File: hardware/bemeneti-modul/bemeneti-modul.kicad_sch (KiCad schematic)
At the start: 112 parts, among them J301 IN0, J302 IN1, J303 IN2, J304 IN3, J305 IN4, J306 IN5, J307 IN6, J308 IN7, J309 IN8, J310 IN9, J311 IN10, J312 IN11, J313 IN12, J314 IN13, J315 IN14, J316 IN15, J320 I2C KÜLSŐ, U301 AP2112K-3.3TRG1, U302 HDC3020DEFR, U303 TPD4E05U06DQAR, U304 TPD4E05U06DQAR, U305 TPD4E05U06DQAR, U306 TPD4E05U06DQAR, U307 TPD4E05U06DQAR

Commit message: Hardver: szakértői javítások (D74–D77), STM32L433 + SN65HVD230 + GND-ági polaritásvédelem (D78–D81), teljes ellenőrzés
- D74–D77: busz-GND ellenállás, CAN-fojtó-hely, TVS a +5V_BUCK-on és a VUSB-n, bemenetvédelem,
  230 V-os és antenna-tiltás a NYÁK-on, SCT-jack footprint
- D78–D80: modul-MCU STM32L433RCT3 (VIN_SENSE PB1, LED: TIM15/TIM16, I_SENSE PA3), modul-transceiver
  SN65HVD230, N-FET a GND-ágban (vezérlő Q1, LED Q201, relé Q100), MCP9701A, táp-LED a +5V-ról,
  2 oz a LED-/relémodulon, AP2112K marad; D81 javaslat (TPD4E02B04 a bemeneteken)
- CubeMX-projektek L433-ra, fejsoros kódgenerálással ellenőrizve (minden periféria inicializálódik)
- gen/ellenorzes.py (ERC, láb ↔ pad, modulmag, CubeMX, polaritásvédelem, NYÁK ↔ rajz, DRC) – 0 hiba
- gen/bom.sh + bom/*.csv darabjegyzék; docs/komponenslista.md a konzulensnek
- kontextus: DONTESEK D74–D81, specifikációk, ATTEKINTES, NAPLO, beszerzési lista; alkatrészkészlet-jegyzet (claude.ai)

Co-Authored-By: Claude Opus 5.5 <noreply@anthropic.com>
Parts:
- added R390: 0R, Resistor_SMD:R_1206_3216Metric, symbol Device:R
- R310, R311, R312, R313, R314, R315, R316, R317, R318, R319, R320, R321, R322, R323, R324, R325: value 1k -> 10k; Megjegyzés (none) -> soros: 24 V-os félrekötésnél ~2 mA az ESD-tömbbe (U303–U306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
- R330, R331, R332, R333, R334, R335, R336, R337, R338, R339, R340, R341, R342, R343, R344, R345: Megjegyzés (none) -> felhúzás a csatlakozó oldalán (D75); 12/24 V-os jelnél kive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
- U302: Megjegyzés (none) -> a ház belsejének klímáját méri (elosztószekrény), nem a szo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
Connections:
- net GND: now also R390.2
- net IN0: no longer R330.2
- net IN1: no longer R331.2
- net IN10: no longer R340.2
- net IN11: no longer R341.2
- net IN12: no longer R342.2
- net IN13: no longer R343.2
- net IN14: no longer R344.2
- net IN15: no longer R345.2
- net IN2: no longer R332.2
- net IN3: no longer R333.2
- net IN4: no longer R334.2
- net IN5: no longer R335.2
- net IN6: no longer R336.2
- net IN7: no longer R337.2
- net IN8: no longer R338.2
- net IN9: no longer R339.2
- net at J306.3 (Pin_3), R315.1: now also R335.2
- net at J301.3 (Pin_3), R310.1: now also R330.2
- net at J315.3 (Pin_3), R324.1: now also R344.2
- net at J302.3 (Pin_3), R311.1: now also R331.2
- net at J309.3 (Pin_3), R318.1: now also R338.2
- net at J311.3 (Pin_3), R320.1: now also R340.2
- net at J307.3 (Pin_3), R316.1: now also R336.2
- net at J304.3 (Pin_3), R313.1: now also R333.2
- net at J312.3 (Pin_3), R321.1: now also R341.2
- net at J305.3 (Pin_3), R314.1: now also R334.2
- net at J314.3 (Pin_3), R323.1: now also R343.2
- net at J313.3 (Pin_3), R322.1: now also R342.2
- net at J303.3 (Pin_3), R312.1: now also R332.2
- net at J310.3 (Pin_3), R319.1: now also R339.2
- net at J308.3 (Pin_3), R317.1: now also R337.2
- net at J316.3 (Pin_3), R325.1: now also R345.2
- new net GND_BUS: R390.1
- no-connect marks 28 -> 26
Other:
- sheet modulmag ports: added GND_BUS, PB1; removed PC6, PC7, PC8
- note added: "2. BEMENETEK (× 16): PH 1 = táp (SUPk), 2 = GND, 3 = JEL → R_fel a 3,3 V-ra (csatlakozó-oldal) → R_s → csomópont (R_le (DNP), C) → MCU; ESD az MCU-oldalon"
- note added: "Alap: R_fel 10k + R_s 10k + C 10n (D75) – félrekötött 24 V-nál ~2 mA az ESD-tömbbe, a láb ~VBR-en (D81!). 12/24 V-os jel: R_fel ki, R_s 68k, R_le 10k; 5 V: R_s 2k2, R_le 3k9."
- note removed: "2. BEMENETEK (× 16): PH 1 = táp (SUPk), 2 = GND, 3 = JEL → R_s → csomópont (R_fel a 3,3 V-ra, R_le (DNP) és C a GND-re) → MCU; ESD az MCU-oldalon (lent)"
- note removed: "Alap: R_s 1k + R_fel 10k + C 10n → érintkező, reed, gomb, open-drain (pl. AH1911), 3,3 V-os kimenet. 12/24 V-os jel: R_s 68k, R_le 10k, R_fel ki."

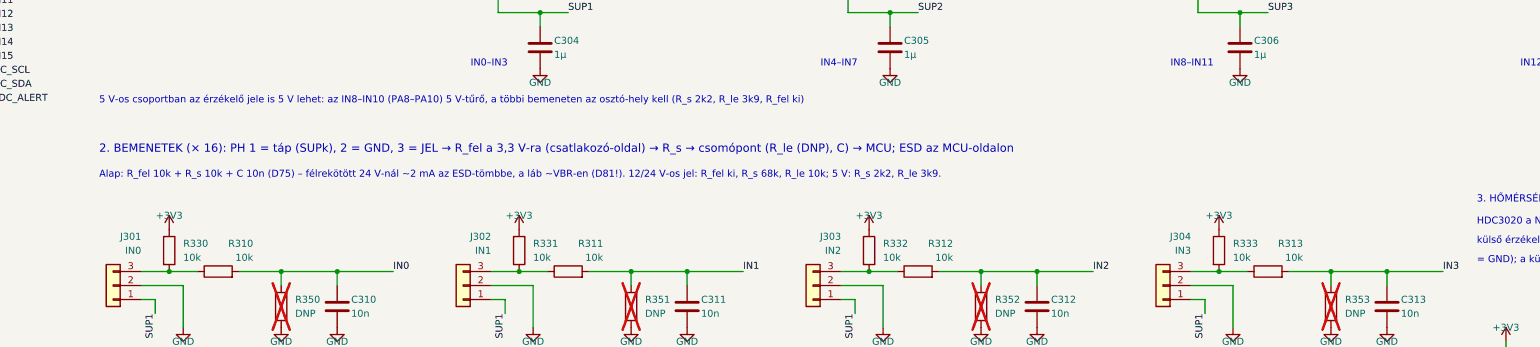
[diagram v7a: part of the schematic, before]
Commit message: Hardver: relékimenet 5,08 mm-es THT sorkapocs (D83), D81 elvetve – marad a TPD4E05U06
Co-Authored-By: Claude Opus 5.5 <noreply@anthropic.com>
Claude-Session: https://claude.ai/code/session_01KVtZMUPbtveTXy9VyJshyt
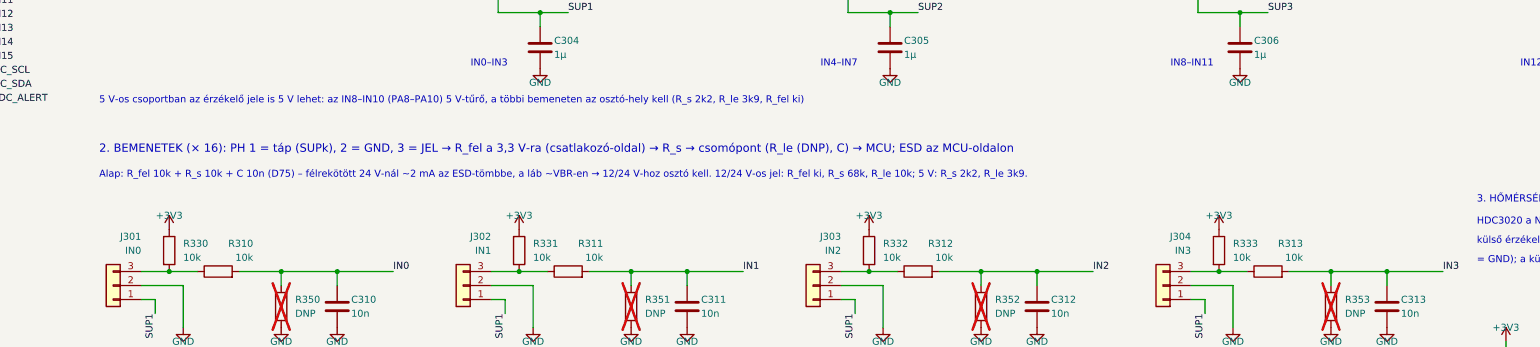
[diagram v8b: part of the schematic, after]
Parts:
- R310, R311, R312, R313, R314, R315, R316, R317, R318, R319, R320, R321, R322, R323, R324, R325: Megjegyzés soros: 24 V-os félrekötésnél ~2 mA az ESD-tömbbe (U303–U306), a láb a letörési feszültségén – D75, D81; 12/24 V-os osztóhoz 68k -> soros: 24 V-os félrekötésnél ~2 mA az ESD-tömbbe (U303–U306), a láb a letörési feszültségén (D75) – 12/24 V-os jelhez osztó (68k)
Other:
- note added: "Alap: R_fel 10k + R_s 10k + C 10n (D75) – félrekötött 24 V-nál ~2 mA az ESD-tömbbe, a láb ~VBR-en → 12/24 V-hoz osztó kell. 12/24 V-os jel: R_fel ki, R_s 68k, R_le 10k; 5 V: R_s 2k2, R_le 3k9."
- note removed: "Alap: R_fel 10k + R_s 10k + C 10n (D75) – félrekötött 24 V-nál ~2 mA az ESD-tömbbe, a láb ~VBR-en (D81!). 12/24 V-os jel: R_fel ki, R_s 68k, R_le 10k; 5 V: R_s 2k2, R_le 3k9."
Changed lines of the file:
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@@
 		)
 	)
-	(text "Alap: R_fel 10k + R_s 10k + C 10n (D75) – félrekötött 24 V-nál ~2 mA az ESD-tömbbe, a láb ~VBR-en (D81!). 12/24 V-os jel: R_fel ki, R_s 68k, R_le 10k; 5 V: R_s 2k2, R_le 3k9."
+	(text "Alap: R_fel 10k + R_s 10k + C 10n (D75) – félrekötött 24 V-nál ~2 mA az ESD-tömbbe, a láb ~VBR-en → 12/24 V-hoz osztó kell. 12/24 V-os jel: R_fel ki, R_s 68k, R_le 10k; 5 V: R_s 2k2, R_le 3k9."
 		(exclude_from_sim no)
 		(at 80 97.5 0)
@@
 			)
 		)
-		(property "Megjegyzés" "soros: 24 V-os félrekötésnél ~2 mA az ESD-tömbbe (U303–U306), a láb a letörési feszültségén – D75, D81; 12/24 V-os osztóhoz 68k"
+		(property "Megjegyzés" "soros: 24 V-os félrekötésnél ~2 mA az ESD-tömbbe (U303–U306), a láb a letörési feszültségén (D75) – 12/24 V-os jelhez osztó (68k)"
 			(at 292.1 172.72 90)
 			(hide yes)
@@
 			)
 		)
-		(property "Megjegyzés" "soros: 24 V-os félrekötésnél ~2 mA az ESD-tömbbe (U303–U306), a láb a letörési feszültségén – D75, D81; 12/24 V-os osztóhoz 68k"
+		(property "Megjegyzés" "soros: 24 V-os félrekötésnél ~2 mA az ESD-tömbbe (U303–U306), a láb a letörési feszültségén (D75) – 12/24 V-os jelhez osztó (68k)"
 			(at 101.6 201.93 90)
 			(hide yes)
@@
 			)
 		)
-		(property "Megjegyzés" "soros: 24 V-os félrekötésnél ~2 mA az ESD-tömbbe (U303–U306), a láb a letörési feszültségén – D75, D81; 12/24 V-os osztóhoz 68k"
+		(property "Megjegyzés" "soros: 24 V-os félrekötésnél ~2 mA az ESD-tömbbe (U303–U306), a láb a letörési feszültségén (D75) – 12/24 V-os jelhez osztó (68k)"
 			(at 228.6 114.3 90)
 			(hide yes)
@@
 			)
 		)
-		(property "Megjegyzés" "soros: 24 V-os félrekötésnél ~2 mA az ESD-tömbbe (U303–U306), a láb a letörési feszültségén – D75, D81; 12/24 V-os osztóhoz 68k"
+		(property "Megjegyzés" "soros: 24 V-os félrekötésnél ~2 mA az ESD-tömbbe (U303–U306), a láb a letörési feszültségén (D75) – 12/24 V-os jelhez osztó (68k)"
 			(at 292.1 201.93 90)
 			(hide yes)
@@
 			)
 		)
-		(property "Megjegyzés" "soros: 24 V-os félrekötésnél ~2 mA az ESD-tömbbe (U303–U306), a láb a letörési feszültségén – D75, D81; 12/24 V-os osztóhoz 68k"
+		(property "Megjegyzés" "soros: 24 V-os félrekötésnél ~2 mA az ESD-tömbbe (U303–U306), a láb a letörési feszültségén (D75) – 12/24 V-os jelhez osztó (68k)"
 			(at 228.6 143.51 90)
 			(hide yes)
@@
 			)
 		)
-		(property "Megjegyzés" "soros: 24 V-os félrekötésnél ~2 mA az ESD-tömbbe (U303–U306), a láb a letörési feszültségén – D75, D81; 12/24 V-os osztóhoz 68k"
+		(property "Megjegyzés" "soros: 24 V-os félrekötésnél ~2 mA az ESD-tömbbe (U303–U306), a láb a letörési feszültségén (D75) – 12/24 V-os jelhez osztó (68k)"
 			(at 292.1 143.51 90)
 			(hide yes)
@@
 			)
 		)
-		(property "Megjegyzés" "soros: 24 V-os félrekötésnél ~2 mA az ESD-tömbbe (U303–U306), a láb a letörési feszültségén – D75, D81; 12/24 V-os osztóhoz 68k"
+		(property "Megjegyzés" "soros: 24 V-os félrekötésnél ~2 mA az ESD-tömbbe (U303–U306), a láb a letörési feszültségén (D75) – 12/24 V-os jelhez osztó (68k)"
 			(at 101.6 172.72 90)
 			(hide yes)
@@
 			)
 		)
-		(property "Megjegyzés" "soros: 24 V-os félrekötésnél ~2 mA az ESD-tömbbe (U303–U306), a láb a letörési feszültségén – D75, D81; 12/24 V-os osztóhoz 68k"
+		(property "Megjegyzés" "soros: 24 V-os félrekötésnél ~2 mA az ESD-tömbbe (U303–U306), a láb a letörési feszültségén (D75) – 12/24 V-os jelhez osztó (68k)"
 			(at 228.6 172.72 90)
 			(hide yes)
@@
 			)
 		)
-		(property "Megjegyzés" "soros: 24 V-os félrekötésnél ~2 mA az ESD-tömbbe (U303–U306), a láb a letörési feszültségén – D75, D81; 12/24 V-os osztóhoz 68k"
+		(property "Megjegyzés" "soros: 24 V-os félrekötésnél ~2 mA az ESD-tömbbe (U303–U306), a láb a letörési feszültségén (D75) – 12/24 V-os jelhez osztó (68k)"
 			(at 101.6 143.51 90)
 			(hide yes)
@@
 			)
 		)
-		(property "Megjegyzés" "soros: 24 V-os félrekötésnél ~2 mA az ESD-tömbbe (U303–U306), a láb a letörési feszültségén – D75, D81; 12/24 V-os osztóhoz 68k"
+		(property "Megjegyzés" "soros: 24 V-os félrekötésnél ~2 mA az ESD-tömbbe (U303–U306), a láb a letörési feszültségén (D75) – 12/24 V-os jelhez osztó (68k)"
 			(at 292.1 114.3 90)
 			(hide yes)
@@
 			)
 		)
-		(property "Megjegyzés" "soros: 24 V-os félrekötésnél ~2 mA az ESD-tömbbe (U303–U306), a láb a letörési feszültségén – D75, D81; 12/24 V-os osztóhoz 68k"
+		(property "Megjegyzés" "soros: 24 V-os félrekötésnél ~2 mA az ESD-tömbbe (U303–U306), a láb a letörési feszültségén (D75) – 12/24 V-os jelhez osztó (68k)"
 			(at 165.1 172.72 90)
 			(hide yes)
@@
 			)
 		)
-		(property "Megjegyzés" "soros: 24 V-os félrekötésnél ~2 mA az ESD-tömbbe (U303–U306), a láb a letörési feszültségén – D75, D81; 12/24 V-os osztóhoz 68k"
+		(property "Megjegyzés" "soros: 24 V-os félrekötésnél ~2 mA az ESD-tömbbe (U303–U306), a láb a letörési feszültségén (D75) – 12/24 V-os jelhez osztó (68k)"
 			(at 101.6 114.3 90)
 			(hide yes)
@@
 			)
 		)
-		(property "Megjegyzés" "soros: 24 V-os félrekötésnél ~2 mA az ESD-tömbbe (U303–U306), a láb a letörési feszültségén – D75, D81; 12/24 V-os osztóhoz 68k"
+		(property "Megjegyzés" "soros: 24 V-os félrekötésnél ~2 mA az ESD-tömbbe (U303–U306), a láb a letörési feszültségén (D75) – 12/24 V-os jelhez osztó (68k)"
 			(at 165.1 114.3 90)
 			(hide yes)
@@
 			)
 		)
-		(property "Megjegyzés" "soros: 24 V-os félrekötésnél ~2 mA az ESD-tömbbe (U303–U306), a láb a letörési feszültségén – D75, D81; 12/24 V-os osztóhoz 68k"
+		(property "Megjegyzés" "soros: 24 V-os félrekötésnél ~2 mA az ESD-tömbbe (U303–U306), a láb a letörési feszültségén (D75) – 12/24 V-os jelhez osztó (68k)"
 			(at 165.1 143.51 90)
 			(hide yes)
@@
 			)
 		)
-		(property "Megjegyzés" "soros: 24 V-os félrekötésnél ~2 mA az ESD-tömbbe (U303–U306), a láb a letörési feszültségén – D75, D81; 12/24 V-os osztóhoz 68k"
+		(property "Megjegyzés" "soros: 24 V-os félrekötésnél ~2 mA az ESD-tömbbe (U303–U306), a láb a letörési feszültségén (D75) – 12/24 V-os jelhez osztó (68k)"
 			(at 228.6 201.93 90)
 			(hide yes)
@@
 			)
 		)
-		(property "Megjegyzés" "soros: 24 V-os félrekötésnél ~2 mA az ESD-tömbbe (U303–U306), a láb a letörési feszültségén – D75, D81; 12/24 V-os osztóhoz 68k"
+		(property "Megjegyzés" "soros: 24 V-os félrekötésnél ~2 mA az ESD-tömbbe (U303–U306), a láb a letörési feszültségén (D75) – 12/24 V-os jelhez osztó (68k)"
 			(at 165.1 201.93 90)
 			(hide yes)
